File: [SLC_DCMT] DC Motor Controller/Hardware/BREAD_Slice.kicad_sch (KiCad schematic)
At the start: 46 parts, among them J1 Conn_01x10_Female, J10 Term_PressFit_Phoenix_Contact, J11 Term_PressFit_Phoenix_Contact, J12 Term_PressFit_Phoenix_Contact, J13 Term_PressFit_Phoenix_Contact, J14 Term_PressFit_Phoenix_Contact, J15 Term_PressFit_Phoenix_Contact, J16 Term_PressFit_Phoenix_Contact, J17 Term_PressFit_Phoenix_Contact, J18 I2C_01x04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

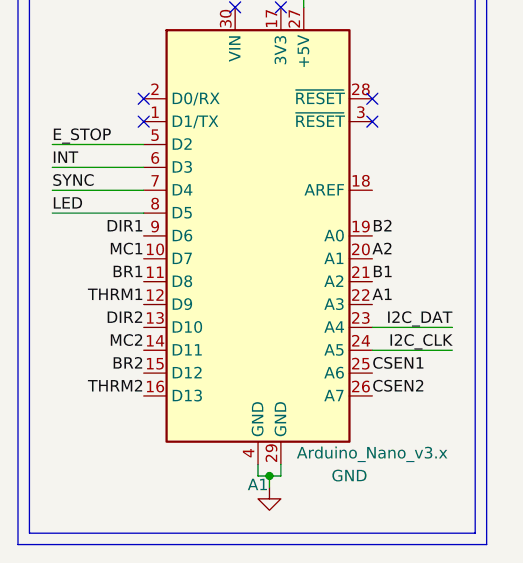
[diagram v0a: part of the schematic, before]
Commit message: Updated DCMT pin connections
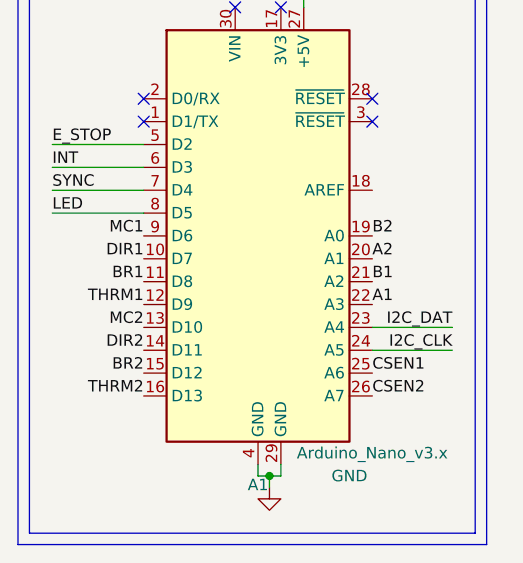
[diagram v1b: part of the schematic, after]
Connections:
- net DIR1: now also A1.10 (D7); no longer A1.9 (D6)
- net DIR2: now also A1.14 (D11); no longer A1.13 (D10)
- net MC1: now also A1.9 (D6); no longer A1.10 (D7)
- net MC2: now also A1.13 (D10); no longer A1.14 (D11)
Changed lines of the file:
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@@
     (effects (font (size 1.27 1.27)) (justify right bottom))
   )
-  (label "DIR1" (at 30.48 161.29 180) (fields_autoplaced)
+  (label "DIR1" (at 30.48 163.83 180) (fields_autoplaced)
     (effects (font (size 1.27 1.27)) (justify right bottom))
   )
@@
     (effects (font (size 1.27 1.27)) (justify left bottom))
   )
-  (label "DIR2" (at 30.48 171.45 180) (fields_autoplaced)
+  (label "DIR2" (at 30.48 173.99 180) (fields_autoplaced)
     (effects (font (size 1.27 1.27)) (justify right bottom))
   )
-  (label "MC2" (at 30.48 173.99 180) (fields_autoplaced)
+  (label "MC2" (at 30.48 171.45 180) (fields_autoplaced)
     (effects (font (size 1.27 1.27)) (justify right bottom))
   )
@@
     (effects (font (size 1.27 1.27)) (justify right bottom))
   )
-  (label "MC1" (at 30.48 163.83 180) (fields_autoplaced)
+  (label "MC1" (at 30.48 161.29 180) (fields_autoplaced)
     (effects (font (size 1.27 1.27)) (justify right bottom))
   )
